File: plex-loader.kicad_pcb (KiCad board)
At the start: 4 copper layers, 38.1 x 68 mm, 48 parts, among them J1 Conn_01x05_Pin, J10 Conn_02x05_Odd_Even, J2 Conn_01x05_Pin, J3 Conn_01x05_Pin, J4 Conn_01x05_Pin, J5 Conn_01x05_Pin, J6 Conn_01x05_Pin, J9 Conn_02x20_Odd_Even, U1 TMUX1208PWR, U2 TMUX1208PWR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

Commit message: curtis changes
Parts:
- D1, D2, D3, D4, D5, D6, D7, D8, D9: footprint LED_SMD:LED_0603_1608Metric -> LED_SMD:LED_0805_2012Metric
- R11, R12, R13, R14, R15, R16, R17, R18: value 50 -> 1k
- moved U5 43.2 mm to (72.4, 55.3), turned to 90 degrees
- moved R3 42.6 mm to (72.4, 58.9), turned to 0 degrees
- moved R4 20.8 mm to (81.3, 110.3), turned to 90 degrees
- moved D1 17.7 mm to (81.3, 106.8), turned to -90 degrees
- moved C3 8.78 mm to (71.5, 96.7)
- moved U3 8.71 mm to (66.5, 97.5)
- moved R7 8.25 mm to (69.0, 93.2), turned to 0 degrees
- moved C2 5.23 mm to (71.5, 84.7)
- moved U2 5.14 mm to (66.5, 85.5)
- moved R8 4.63 mm to (69.5, 81.2)
- moved R18 2.21 mm to (76.3, 110.3)
- moved D9 2.00 mm to (76.3, 106.8)
- moved R17 1.90 mm to (78.8, 110.3)
- moved G*** 1.80 mm to (67.5, 109.0)
- moved D8 1.66 mm to (78.8, 106.8)
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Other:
- board text added: "Stat 1"
- board text added: "Stat 2"
- board text removed: "Status 1"
- board text removed: "Status 2"

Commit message: route draft
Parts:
- moved R9 8.52 mm to (69.5, 77.7)
- moved R7 8.52 mm to (69.7, 101.7)
- moved R8 8.50 mm to (69.5, 89.7)
- moved G*** 1.24 mm to (67.2, 110.2)
- turned R4 to -90 degrees
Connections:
- U4 pad 21: /PDG8 -> /PGD8
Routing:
- net /GPIO10: track 0.00 -> 66.0 mm, vias 0 -> 3
- net /GPIO2: track 0.00 -> 62.6 mm, vias 0 -> 1
- net /dspic/B3: track 0.00 -> 60.2 mm, vias 0 -> 1
- net /MCLR6: track 0.00 -> 56.3 mm, vias 0 -> 2
- net /GPIO3: track 0.00 -> 54.5 mm, vias 0 -> 2
- net /GPIO22: track 0.00 -> 54.1 mm, vias 0 -> 1
- net /GPIO17: track 0.00 -> 47.6 mm, vias 0 -> 3
- net /dspic/B4: track 0.00 -> 46.4 mm, vias 0 -> 3
- net /PGC1: track 0.00 -> 44.8 mm
- net /GPIO27: track 0.00 -> 43.8 mm, vias 0 -> 1
- net /MCLR8: track 0.00 -> 41.7 mm, vias 0 -> 1
- net /PGD6: track 0.00 -> 41.0 mm, vias 0 -> 2
- net /PGC2: track 0.00 -> 39.0 mm, vias 0 -> 2
- net /MCLR5: track 0.00 -> 38.0 mm, vias 0 -> 1
- net /GPIO23: track 0.00 -> 35.4 mm, vias 0 -> 2
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
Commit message: trace touchup
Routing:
- net /MCLR2: track 13.5 -> 12.3 mm
- net VDD: track 17.1 -> 18.2 mm
- net GND: track 15.5 -> 16.3 mm
- net /GPIO2: track 62.6 -> 63.3 mm
- net /GPIO23: track 35.4 -> 34.8 mm

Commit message: fix res val
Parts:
- R4: value 50 -> 1k
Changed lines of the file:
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@@
 		(fp_text user "*"
 			(at -3.2068 -3.768801 0)
-			(unlocked yes)
 			(layer "F.SilkS")
 			(effects
@@
 		(fp_text user "*"
 			(at -3.2068 -3.768801 0)
+			(unlocked yes)
 			(layer "F.SilkS")
 			(effects
@@
 			)
 		)
-		(fp_text user "${REFERENCE}"
-			(at 0 0 0)
-			(unlocked yes)
+		(fp_text user "*"
+			(at -1.869001 -2.4738 0)
 			(layer "F.Fab")
 			(effects
@@
 			)
 		)
-		(fp_text user "*"
-			(at -1.869001 -2.4738 0)
+		(fp_text user "${REFERENCE}"
+			(at 0 0 0)
+			(unlocked yes)
 			(layer "F.Fab")
 			(effects
@@
 			)
 		)
-		(property "Value" "50"
+		(property "Value" "1k"
 			(at 1.175 -2 360)
 			(layer "F.Fab")
@@
 		(fp_text user "*"
 			(at -3.2068 -3.768801 0)
+			(unlocked yes)
 			(layer "F.SilkS")
 			(effects
@@
 		(fp_text user "*"
 			(at -3.2068 -3.768801 0)
-			(unlocked yes)
 			(layer "F.SilkS")
 			(effects
@@
 		(fp_text user "*"
 			(at -1.869001 -2.4738 0)
+			(unlocked yes)
 			(layer "F.Fab")
 			(effects
@@
 		(fp_text user "*"
 			(at -1.869001 -2.4738 0)
-			(unlocked yes)
 			(layer "F.Fab")
 			(effects
@@
 		(fp_text user "*"
 			(at -3.2068 -3.768801 0)
+			(unlocked yes)
 			(layer "F.SilkS")
 			(effects
@@
 		(fp_text user "*"
 			(at -3.2068 -3.768801 0)
-			(unlocked yes)
 			(layer "F.SilkS")
 			(effects
@@
 			)
 		)
-		(fp_text user "*"
-			(at -1.869001 -2.4738 0)
+		(fp_text user "${REFERENCE}"
+			(at 0 0 0)
 			(unlocked yes)
 			(layer "F.Fab")
@@
 		(fp_text user "*"
 			(at -1.869001 -2.4738 0)
+			(unlocked yes)
 			(layer "F.Fab")
 			(effects
@@
 			)
 		)
-		(fp_text user "${REFERENCE}"
-			(at 0 0 0)
-			(unlocked yes)
+		(fp_text user "*"
+			(at -1.869001 -2.4738 0)
 			(layer "F.Fab")
 			(effects

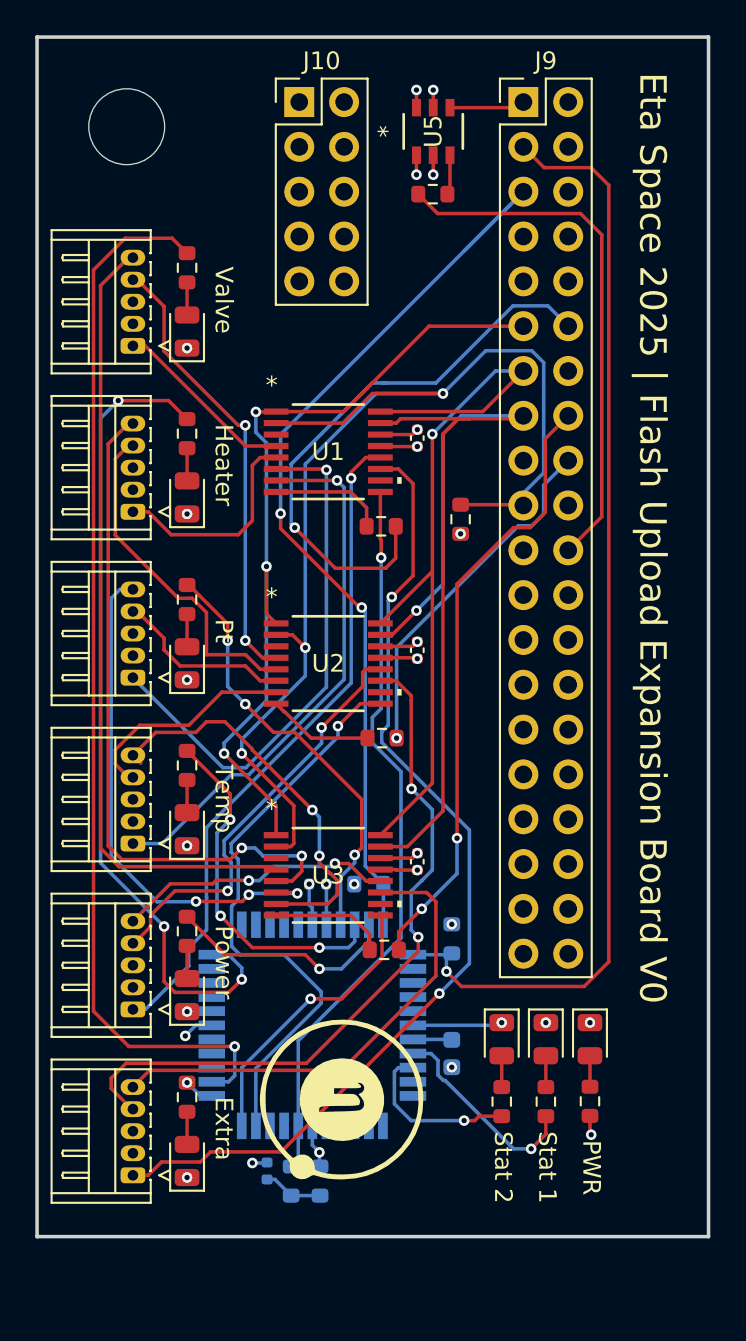
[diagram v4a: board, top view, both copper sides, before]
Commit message: removed pad via
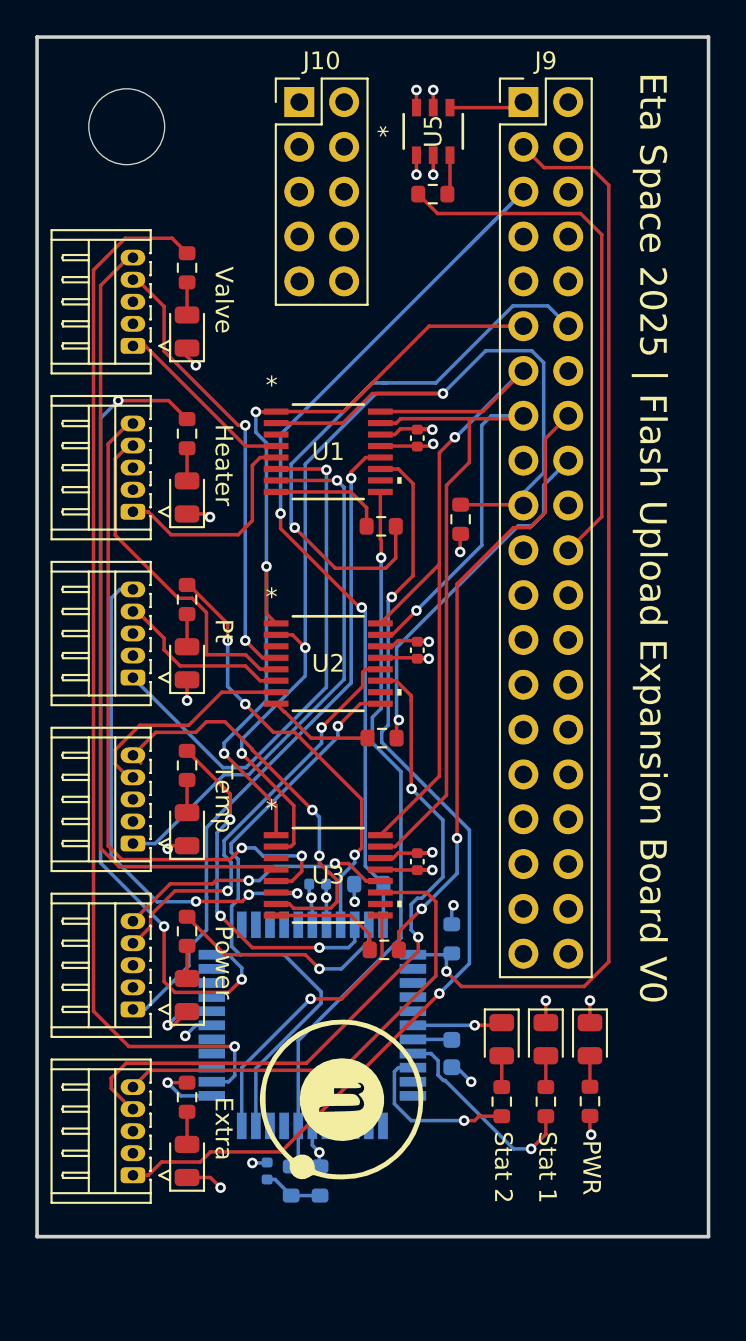
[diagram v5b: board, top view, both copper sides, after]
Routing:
- net GND: track 16.3 -> 36.1 mm
- net VDD: track 18.2 -> 24.3 mm
- net /dspic/B2: track 1.71 -> 3.91 mm
- net /GPIO22: track 54.1 -> 52.3 mm
- net /PGD6: track 40.7 -> 41.3 mm

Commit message: update
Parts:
- added R19: 100, Resistor_SMD:R_0603_1608Metric, F.Cu at (72.4, 61.0)
- moved R3 5.40 mm to (72.4, 53.5), turned to 180 degrees
- moved U5 1.81 mm to (72.4, 57.2)
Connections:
- J9 pad 14: unconnected-(J9-Pin_14-Pad14) -> GND
- J9 pad 17: unconnected-(J9-Pin_17-Pad17) -> +3.3V
- J9 pad 20: unconnected-(J9-Pin_20-Pad20) -> GND
- J9 pad 25: unconnected-(J9-Pin_25-Pad25) -> GND
- J9 pad 30: unconnected-(J9-Pin_30-Pad30) -> GND
- J9 pad 34: unconnected-(J9-Pin_34-Pad34) -> GND
- J9 pad 39: unconnected-(J9-Pin_39-Pad39) -> GND
- J9 pad 9: unconnected-(J9-Pin_9-Pad9) -> GND
- R3 pad 1: /GPIO25 -> +3.3V
- U4 pad 16: unconnected-(U4-AVSS-Pad16) -> GND
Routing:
- net +3.3V: track 4.29 -> 34.0 mm, vias 0 -> 2
- net Net-(U5-G): track 2.27 -> 9.59 mm
- net /GPIO3: track 54.5 -> 49.7 mm
- net +5V: track 0.00 -> 2.54 mm
- net /GPIO25: track 30.0 -> 27.8 mm
- net GND: track 36.1 -> 35.3 mm
